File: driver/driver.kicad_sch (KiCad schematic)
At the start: 3 parts, among them J101 UJC-HP-3-SMT-TR

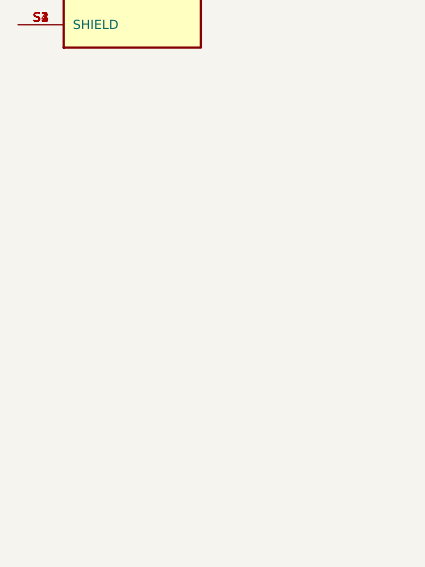
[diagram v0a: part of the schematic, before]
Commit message: Start placing connectors
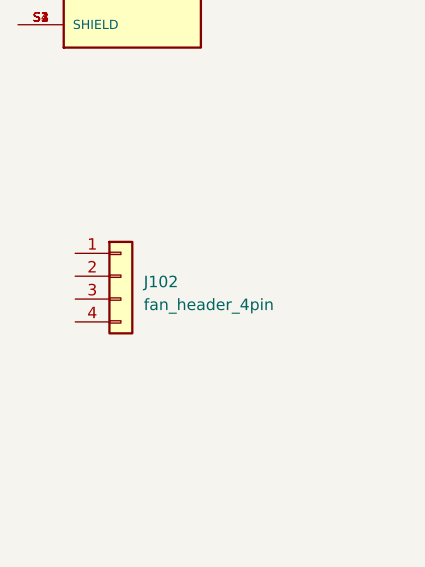
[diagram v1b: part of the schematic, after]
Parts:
- added J102: fan_header_4pin, proj:fan_header_4pin_right_angle, symbol proj:fan_header_4pin
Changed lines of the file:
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@@
     (pin "5")
+  )
+  (symbol (lib_id "proj:fan_header_4pin") (at 40.64 97.79 0) (unit 1)
+    (in_bom yes) (on_board yes) (fields_autoplaced)
+    (property "Reference" "J102" (id 0) (at 43.18 98.4249 0)
+      (effects (font (size 1.27 1.27)) (justify left))
+    )
+    (property "Value" "fan_header_4pin" (id 1) (at 43.18 100.9649 0)
+      (effects (font (size 1.27 1.27)) (justify left))
+    )
+    (property "Footprint" "proj:fan_header_4pin_right_angle" (id 2) (at 40.64 97.79 0)
+      (effects (font (size 1.27 1.27)) hide)
+    )
+    (property "Datasheet" "~" (id 3) (at 40.64 97.79 0)
+      (effects (font (size 1.27 1.27)) hide)
+    )
+    (pin "1")
+    (pin "2")
+    (pin "3")
+    (pin "4")
   )
   (symbol (lib_id "proj:RK1191114001") (at 38.1 34.29 0) (unit 1)
@@
       (reference "J101") (unit 1) (value "UJC-HP-3-SMT-TR") (footprint "proj:UJC-HP-3-SMT-TR")
     )
+    (path "/cd9c19c3-e1ed-41d7-b5f1-201ce2249fd3"
+      (reference "J102") (unit 1) (value "fan_header_4pin") (footprint "proj:fan_header_4pin_right_angle")
+    )
     (path "/6be9453d-3c8b-4f09-87ca-9bc404991b46"

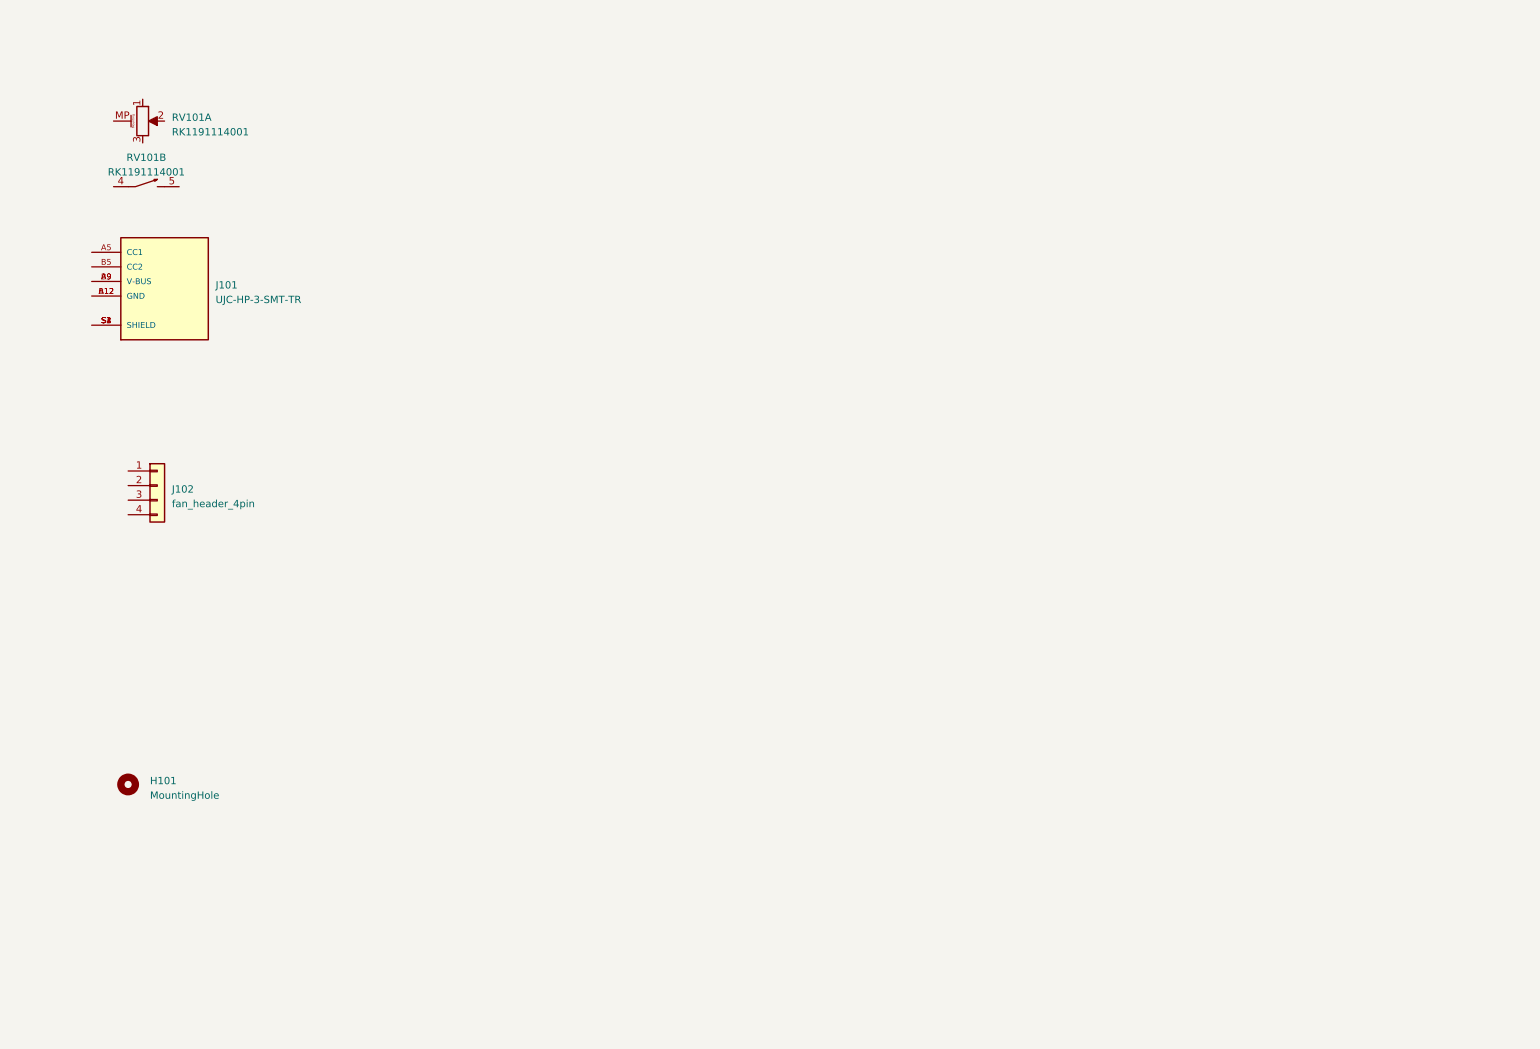
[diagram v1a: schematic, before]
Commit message: First PCB routing
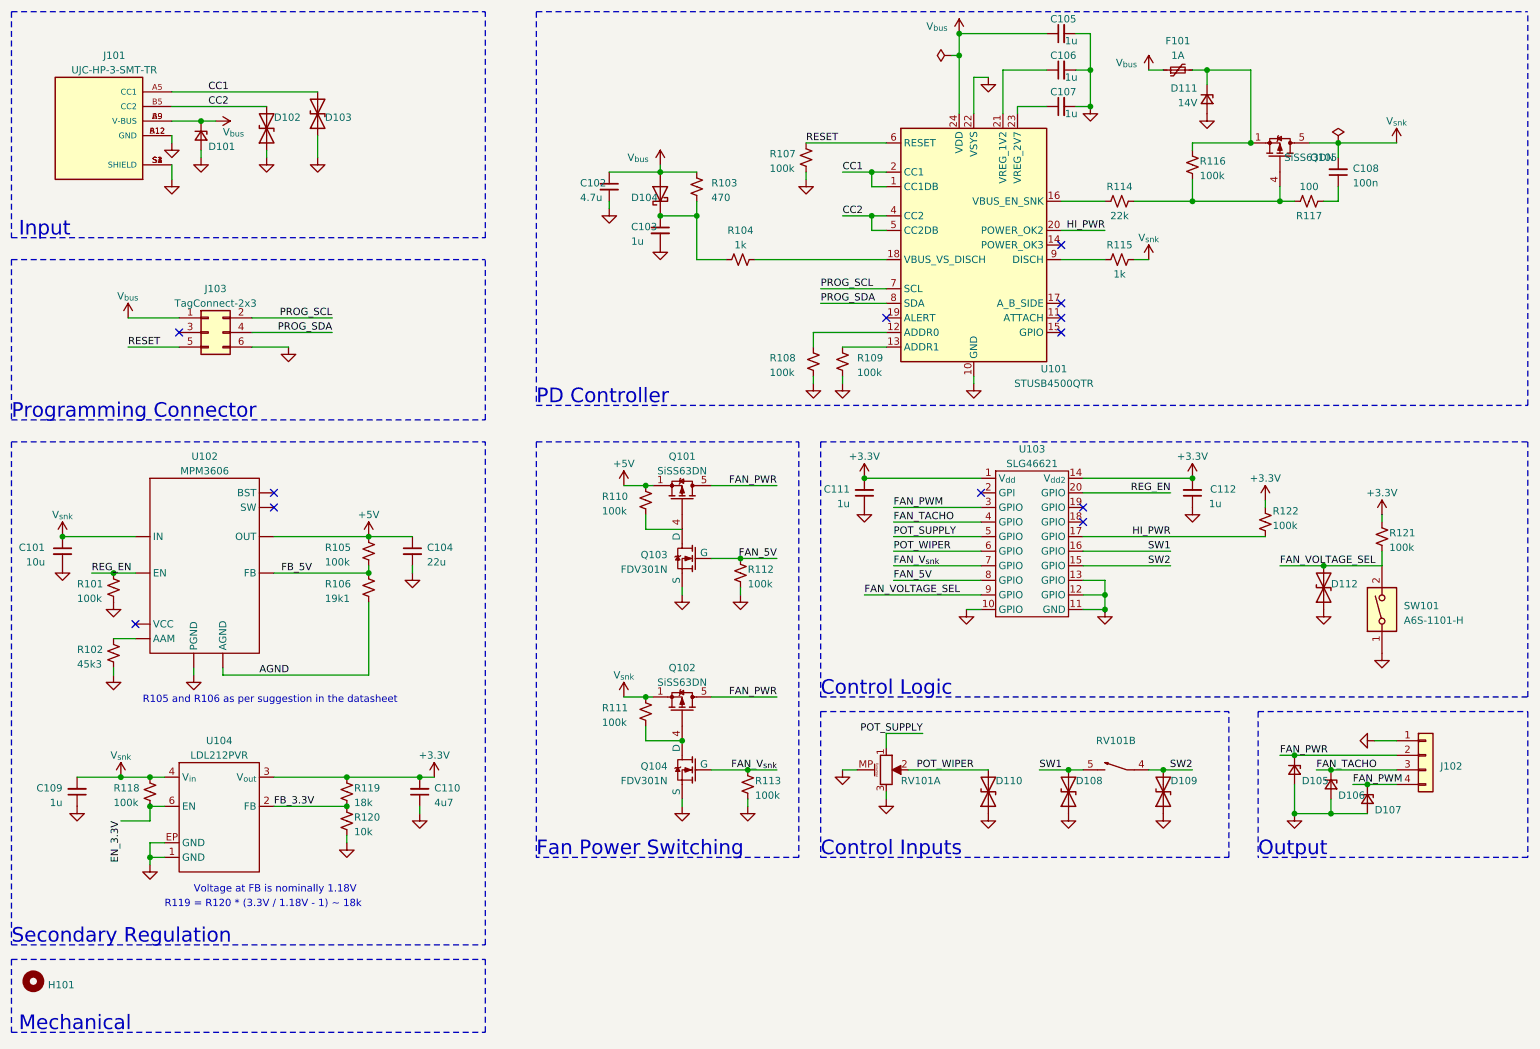
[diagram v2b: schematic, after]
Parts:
- added C101: 10u, proj:C_0805_2012Metric, symbol proj:C
- added C102: 4.7u, proj:C_0805_2012Metric, symbol proj:C
- added C103, C105, C106, C107, C109, C111, C112: 1u, proj:C_0402_1005Metric, symbol proj:C
- added C104: 22u, proj:C_0805_2012Metric, symbol proj:C
- added C108: 100n, proj:C_0402_1005Metric, symbol proj:C
- added C110: 4u7, proj:C_0805_2012Metric, symbol proj:C
- added D101, D105, D106, D107: uclamp2271p, proj:uClampxx71P, symbol proj:uclamp2271p
- added D102, D103, D108, D109, D110, D112: uclamp2411za, proj:uClamp2411ZA, symbol proj:uclamp2411za
- added D104: D_Schottky, proj:Schottky_0402, symbol proj:D_Schottky
- added D111: 14V, proj:SOT-23, symbol proj:D_Zener
- added F101: 1A, proj:R_0805_2012Metric, symbol proj:Polyfuse
- added J103: TagConnect-2x3, proj:Tag-Connect_TC2030-IDC-NL_2x03_P1.27mm_Vertical, symbol proj:TagConnect-2x3
- added Q101, Q102, Q105: SiSS63DN, proj:Vishay_PowerPAK_1212-8_Single, symbol proj:SiSS63DN
- added Q103, Q104: FDV301N, proj:SOT-23, symbol proj:FDV301N
- added R101, R105, R107, R108, R109, R110, R111, R112, R113, R116, R118, R121, R122: 100k, proj:R_0402_1005Metric, symbol proj:Resistor
- added R102: 45k3, proj:R_0402_1005Metric, symbol proj:Resistor
- added R103: 470, proj:R_0402_1005Metric, symbol proj:Resistor
- added R104, R115: 1k, proj:R_0402_1005Metric, symbol proj:Resistor
- added R106: 19k1, proj:R_0402_1005Metric, symbol proj:Resistor
- added R114: 22k, proj:R_0402_1005Metric, symbol proj:Resistor
- added R117: 100, proj:R_0402_1005Metric, symbol proj:Resistor
- added R119: 18k, proj:R_0402_1005Metric, symbol proj:Resistor
- added R120: 10k, proj:R_0402_1005Metric, symbol proj:Resistor
- added SW101: A6S-1101-H, proj:A6S-1101-H, symbol proj:A6S-1101-H
- added U101: STUSB4500QTR, Package_DFN_QFN:QFN-24-1EP_4x4mm_P0.5mm_EP2.7x2.7mm, symbol proj:STUSB4500QTR
- added U102: MPM3606, proj:MPM3606, symbol proj:MPM3606
- added U103: SLG46621, proj:SLG46621V, symbol proj:SLG46621
- added U104: LDL212PVR, proj:LDL212PVR, symbol proj:LDL212PVR
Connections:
- net POT_SUPPLY: now reaches RV101.1
- net POT_SUPPLY: now also U103.5 (GPIO)
- net POT_WIPER: now reaches RV101.2
- net POT_WIPER: now also D110.2 (A2), U103.6 (GPIO)
- net GND: now reaches RV101.3
- net GND: now also J101.A12 (GND), J101.B12 (GND), J101.S1 (SHIELD), J101.S2 (SHIELD), J101.S3 (SHIELD), J101.S4 (SHIELD), J102.1 (Pin_1), RV101.MP (MountPin), C101.2, C102.2, C103.2, C104.2, C105.2, C106.2, C107.2, C109.1, C110.1, C111.1, C112.1, D101.2 (A), D102.1 (A1), D103.1 (A1), D105.2 (A), D106.2 (A), D107.2 (A), D108.1 (A1), D109.1 (A1), D110.1 (A1), D111.1 (A), D112.1 (A1), J103.6 (Pin_6), Q103.2 (S), Q104.2 (S), R101.2, R102.2, R107.2, R108.2, R109.2, R112.2, R113.2, R120.2, SW101.1, U101.10 (GND), U101.22 (VSYS), U101.25 (GND), U102.12 (PGND), U102.13 (PGND), U102.14 (PGND), U103.10 (GPIO), U103.11 (GND), U103.12 (GPIO), U103.13 (GPIO), U104.1 (GND), U104.EP (GND)
- net SW2: now reaches RV101.4
- net SW2: now also D109.2 (A2), U103.15 (GPIO)
- net SW1: now reaches RV101.5
- net SW1: now also D108.2 (A2), U103.16 (GPIO)
- net FAN_PWR: now reaches J102.2 (Pin_2)
- net FAN_PWR: now also D105.1 (K), Q101.5 (D), Q102.5 (D)
- net FAN_TACHO: now reaches J102.3 (Pin_3)
- net FAN_TACHO: now also D106.1 (K), U103.4 (GPIO)
- net FAN_PWM: now reaches J102.4 (Pin_4)
- net FAN_PWM: now also D107.1 (K), U103.3 (GPIO)
- net CC1: now reaches J101.A5 (CC1)
- net CC1: now also D103.2 (A2), U101.1 (CC1DB), U101.2 (CC1)
- net V_{bus}: now reaches J101.A9 (V-BUS), J101.B9 (V-BUS)
- net V_{bus}: now also C102.1, C105.1, D101.1 (K), D104.2 (A), F101.1, J103.1 (Pin_1), R103.1, U101.24 (VDD)
- net CC2: now reaches J101.B5 (CC2)
- net CC2: now also D102.2 (A2), U101.4 (CC2), U101.5 (CC2DB)
- new net: R115.1, U101.9 (DISCH)
- new net: Q101.4 (G), Q103.3 (D), R110.2
- new net: C106.1, U101.21 (VREG_1V2)
- new net: R108.1, U101.12 (ADDR0)
- new net: R109.1, U101.13 (ADDR1)
- new net: R114.1, U101.16 (VBUS_EN_SNK)
- new net: R104.2, U101.18 (VBUS_VS_DISCH)
- new net: C107.1, U101.23 (VREG_2V7)
- new net: Q102.4 (G), Q104.3 (D), R111.2
- new net: D111.3 (K), F101.2, Q105.1 (S), Q105.2 (S), Q105.3 (S), R116.1
- new net: R102.1, U102.18 (AAM)
- new net: Q105.4 (G), R114.2, R116.2, R117.1
- new net: C103.1, D104.1 (K), R103.2, R104.1
- new net: C108.1, R117.2
- new net +3.3V: C110.2, C111.2, C112.2, R119.1, R121.1, R122.1, U103.1 (V_{dd}), U103.14 (V_{dd2}), U104.3 (V_{out})
- new net +5V: C104.1, Q101.1 (S), Q101.2 (S), Q101.3 (S), R105.1, R110.1, U102.7,8,9 (OUT)
- new net AGND: R106.2, U102.3 (AGND)
- new net EN_3.3V: R118.2, U104.6 (EN)
- new net FAN_5V: Q103.1 (G), R112.1, U103.8 (GPIO)
- new net FAN_VOLTAGE_SEL: D112.2 (A2), R121.2, SW101.2, U103.9 (GPIO)
- new net FAN_V_{snk}: Q104.1 (G), R113.1, U103.7 (GPIO)
- new net FB_3.3V: R119.2, R120.1, U104.2 (FB)
- new net FB_5V: R105.2, R106.1, U102.1 (FB)
- new net HI_PWR: R122.2, U101.20 (POWER_OK2), U103.17 (GPIO)
- new net PROG_SCL: J103.2 (Pin_2), U101.7 (SCL)
- new net PROG_SDA: J103.4 (Pin_4), U101.8 (SDA)
- new net REG_EN: R101.1, U102.17 (EN), U103.20 (GPIO)
- new net RESET: J103.5 (Pin_5), R107.1, U101.6 (RESET)
- new net V_{snk}: C101.1, C108.2, C109.2, Q102.1 (S), Q102.2 (S), Q102.3 (S), Q105.5 (D), R111.1, R115.2, R118.1, U102.16 (IN), U104.4 (V_{in})
- no-connect marks 0 -> 12
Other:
- note added: "Control Inputs"
- note added: "Control Logic"
- note added: "Fan Power Switching"
- note added: "Input"
- note added: "Mechanical"
- note added: "Output"
- note added: "PD Controller"
- note added: "Programming Connector"
- note added: "R105 and R106 as per suggestion in the datasheet"
- note added: "R119 = R120 * (3.3V / 1.18V - 1) ~~ 18k"
- note added: "Secondary Regulation"
- note added: "Voltage at FB is nominally 1.18V"
- moved on the sheet: H101, J101, J102, RV101A, RV101B

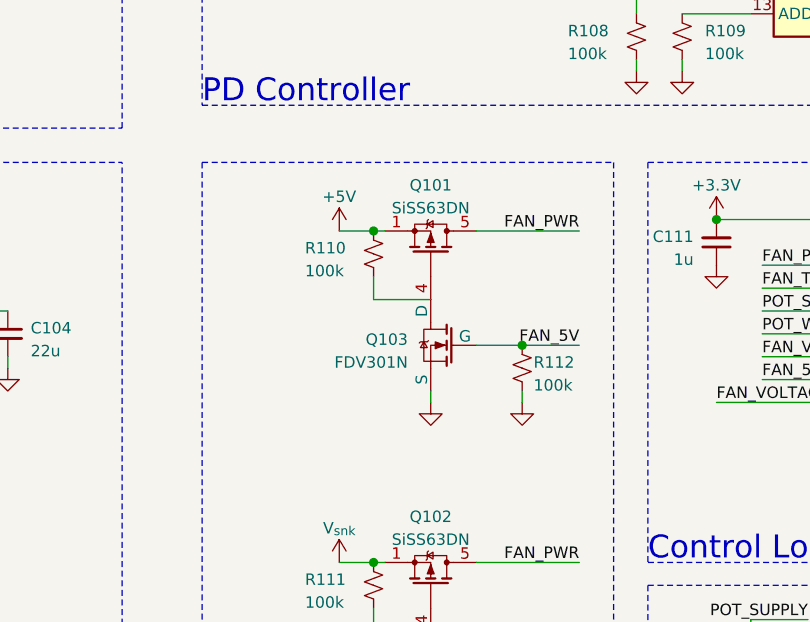
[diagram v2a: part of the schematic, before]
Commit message: Change the 5V power switch mosfet to a controller with reverse voltage protection
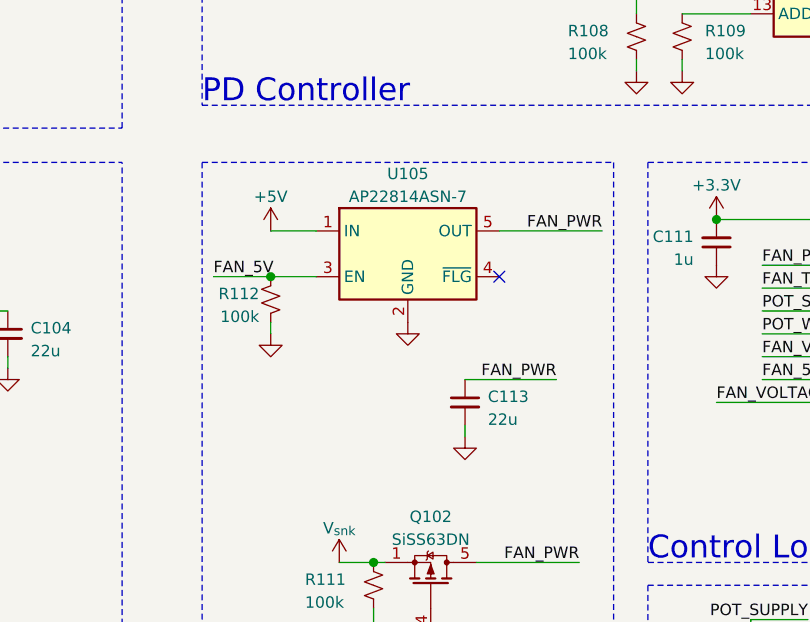
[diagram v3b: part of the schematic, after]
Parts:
- removed Q101: SiSS63DN, proj:Vishay_PowerPAK_1212-8_Single, symbol proj:SiSS63DN
- removed Q103: FDV301N, proj:SOT-23, symbol proj:FDV301N
- removed R110: 100k, proj:R_0402_1005Metric, symbol proj:Resistor
- added C113: 22u, proj:C_0805_2012Metric, symbol proj:C
- added U105: AP22814ASN-7, proj:Diodes_UDFN2020-6, symbol proj:AP22814AW5
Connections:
- net +5V: now also U105.1 (IN)
- net FAN_5V: now also U105.3 (EN)
- net FAN_PWR: now also C113.1, U105.5 (OUT)
- net GND: now also C113.2, U105.2 (GND), U105.EP (GND)
- no-connect marks 12 -> 13
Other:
- moved on the sheet: R112

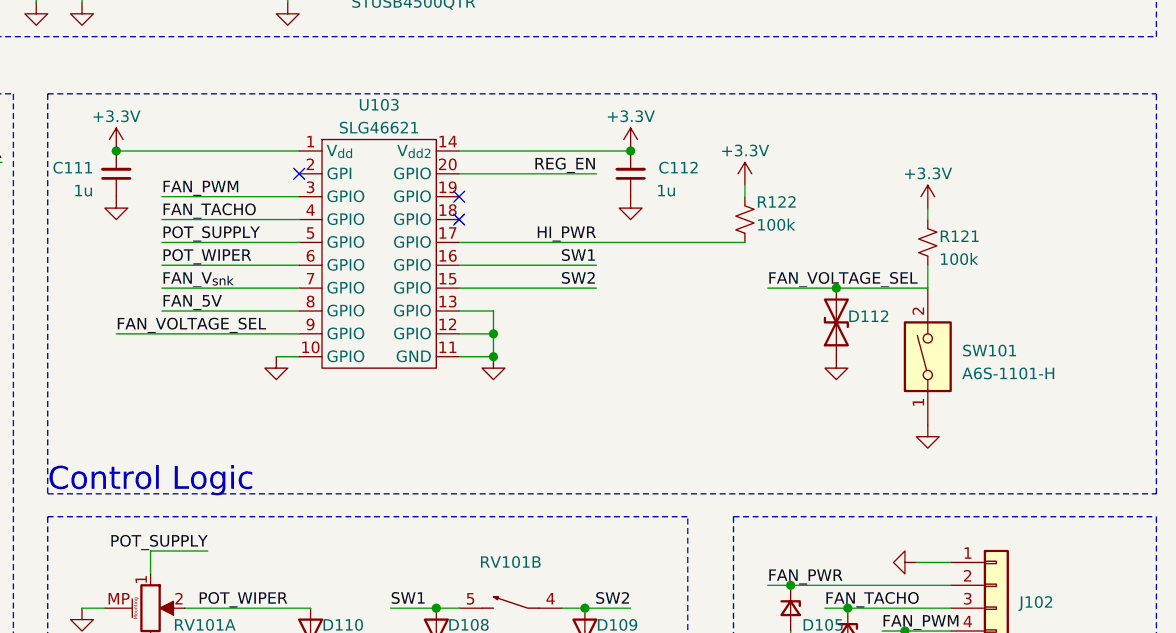
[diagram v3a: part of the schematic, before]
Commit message: FAN_PWM: guard against high voltage from the fan
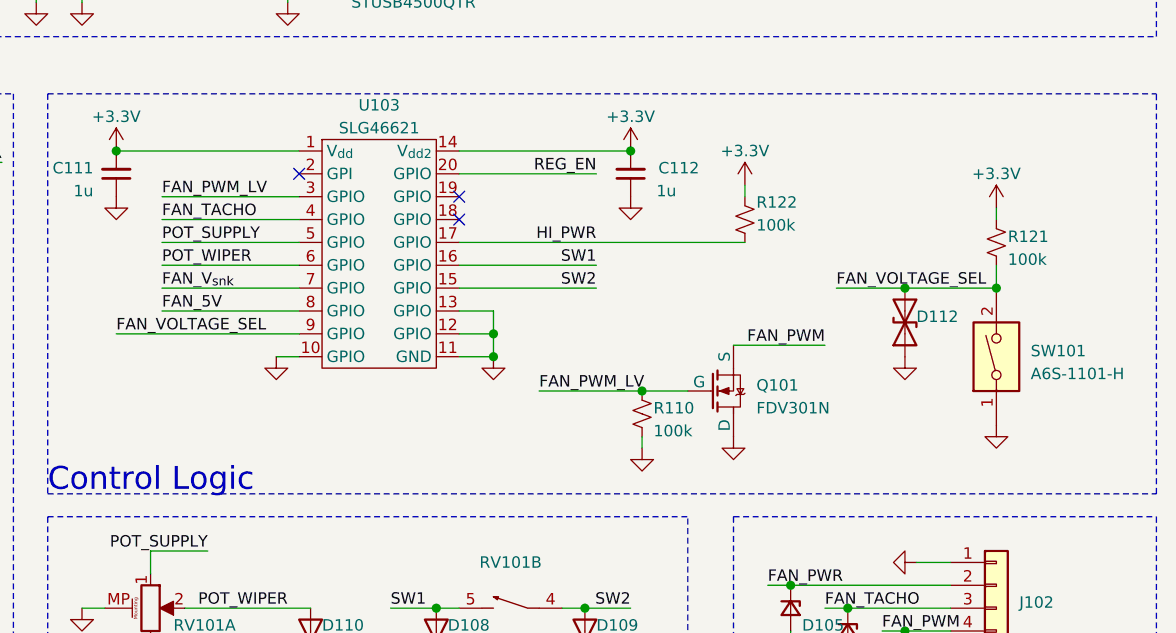
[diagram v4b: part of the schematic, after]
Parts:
- added Q101: FDV301N, proj:SOT-23, symbol proj:FDV301N
- added R110: 100k, proj:R_0402_1005Metric, symbol proj:Resistor
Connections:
- net FAN_PWM: now also Q101.2 (S); no longer U103.3 (GPIO)
- net GND: now also Q101.3 (D), R110.2
- new net FAN_PWM_LV: Q101.1 (G), R110.1, U103.3 (GPIO)
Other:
- moved on the sheet: D112, R121, SW101
